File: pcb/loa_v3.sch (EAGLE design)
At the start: 111 parts, among them IC1 STM32F10XVXT6, IC2 M25P80MW, IC3 S34ML04G100TFI000, IC4 MCP1825S-1202E/DB, IC5 NCP3170, IC6 AD7265SU, Q2 50.000, Q3 25.000, U1 6SLX9TQG144, X3 MINI-USB

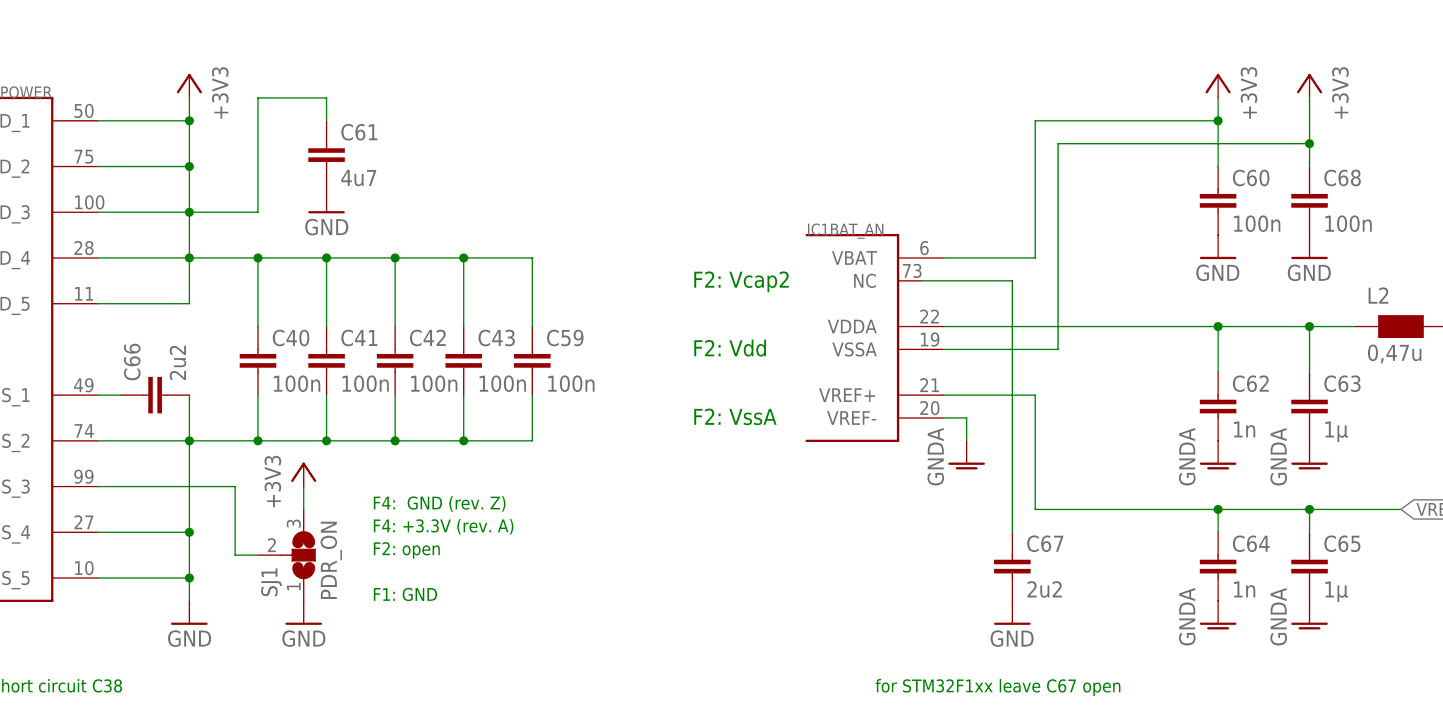
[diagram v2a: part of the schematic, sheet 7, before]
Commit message: Update NAND Flash Package, Reduces C type variations
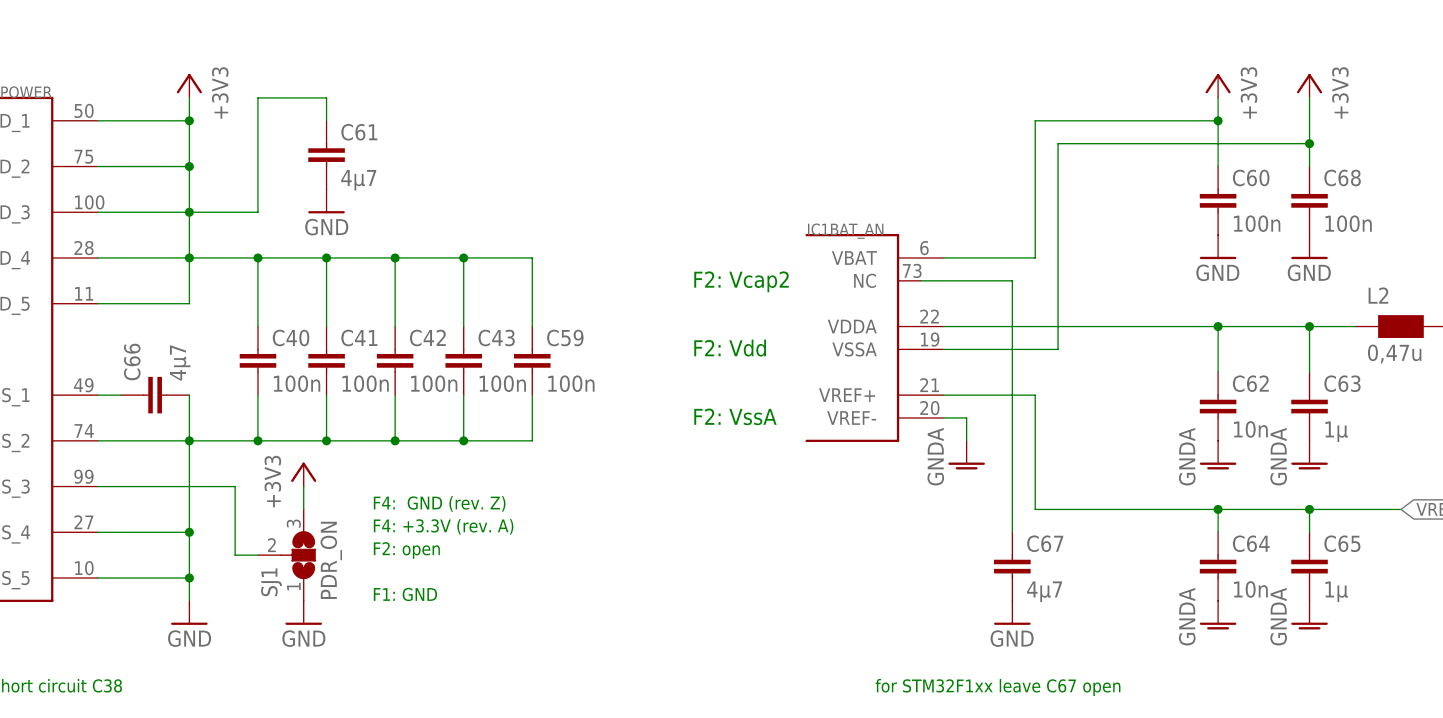
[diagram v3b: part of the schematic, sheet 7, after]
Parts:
- C61: value 4u7 -> 4µ7
- C62, C64: value 1n -> 10n
- C66, C67: value 2u2 -> 4µ7; REICHELT# X7R-G0805 2,2/25 -> X5R-G0805 4,7
- R1: value 820 -> 2k2
- R7: value 10k -> 2k2; device rcl:R-EU_R0603 -> rcl:R-EU_R0805
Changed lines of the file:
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@@
 <?xml version="1.0" encoding="utf-8"?>
 <!DOCTYPE eagle SYSTEM "eagle.dtd">
-<eagle version="6.4">
+<eagle version="6.5.0">
 <drawing>
 <settings>
@@
 <grid distance="0.1" unitdist="inch" unit="inch" style="lines" multiple="1" display="no" altdistance="0.01" altunitdist="inch" altunit="inch"/>
 <layers>
-<layer number="1" name="Top" color="4" fill="1" visible="no" active="no"/>
-<layer number="2" name="Route2" color="1" fill="3" visible="no" active="no"/>
-<layer number="3" name="Route3" color="11" fill="1" visible="no" active="no"/>
-<layer number="4" name="Route4" color="1" fill="4" visible="no" active="no"/>
-<layer number="5" name="Route5" color="4" fill="4" visible="no" active="no"/>
-<layer number="6" name="Route6" color="1" fill="8" visible="no" active="no"/>
-<layer number="7" name="Route7" color="4" fill="8" visible="no" active="no"/>
-<layer number="8" name="Route8" color="1" fill="2" visible="no" active="no"/>
-<layer number="9" name="Route9" color="4" fill="2" visible="no" active="no"/>
-<layer number="10" name="Route10" color="1" fill="7" visible="no" active="no"/>
-<layer number="11" name="Route11" color="4" fill="7" visible="no" active="no"/>
-<layer number="12" name="Route12" color="1" fill="5" visible="no" active="no"/>
-<layer number="13" name="Route13" color="4" fill="5" visible="no" active="no"/>
-<layer number="14" name="Route14" color="1" fill="6" visible="no" active="no"/>
-<layer number="15" name="Route15" color="11" fill="6" visible="no" active="no"/>
-<layer number="16" name="Bottom" color="1" fill="1" visible="no" active="no"/>
-<layer number="17" name="Pads" color="2" fill="1" visible="no" active="no"/>
-<layer number="18" name="Vias" color="2" fill="1" visible="no" active="no"/>
-<layer number="19" name="Unrouted" color="6" fill="1" visible="no" active="no"/>
-<layer number="20" name="Dimension" color="15" fill="1" visible="no" active="no"/>
-<layer number="21" name="tPlace" color="7" fill="1" visible="no" active="no"/>
-<layer number="22" name="bPlace" color="7" fill="1" visible="no" active="no"/>
-<layer number="23" name="tOrigins" color="15" fill="1" visible="no" active="no"/>
-<layer number="24" name="bOrigins" color="15" fill="1" visible="no" active="no"/>
-<layer number="25" name="tNames" color="7" fill="1" visible="no" active="no"/>
-<layer number="26" name="bNames" color="7" fill="1" visible="no" active="no"/>
-<layer number="27" name="tValues" color="7" fill="1" visible="no" active="no"/>
-<layer number="28" name="bValues" color="7" fill="1" visible="no" active="no"/>
+<layer number="1" name="Top" color="4" fill="1" visible="yes" active="no"/>
+<layer number="2" name="Route2" color="1" fill="3" visible="yes" active="no"/>
+<layer number="3" name="Route3" color="11" fill="1" visible="yes" active="no"/>
+<layer number="4" name="Route4" color="1" fill="4" visible="yes" active="no"/>
+<layer number="5" name="Route5" color="4" fill="4" visible="yes" active="no"/>
+<layer number="6" name="Route6" color="1" fill="8" visible="yes" active="no"/>
+<layer number="7" name="Route7" color="4" fill="8" visible="yes" active="no"/>
+<layer number="8" name="Route8" color="1" fill="2" visible="yes" active="no"/>
+<layer number="9" name="Route9" color="4" fill="2" visible="yes" active="no"/>
+<layer number="10" name="Route10" color="1" fill="7" visible="yes" active="no"/>
+<layer number="11" name="Route11" color="4" fill="7" visible="yes" active="no"/>
+<layer number="12" name="Route12" color="1" fill="5" visible="yes" active="no"/>
+<layer number="13" name="Route13" color="4" fill="5" visible="yes" active="no"/>
+<layer number="14" name="Route14" color="1" fill="6" visible="yes" active="no"/>
+<layer number="15" name="Route15" color="11" fill="6" visible="yes" active="no"/>
+<layer number="16" name="Bottom" color="1" fill="1" visible="yes" active="no"/>
+<layer number="17" name="Pads" color="2" fill="1" visible="yes" active="no"/>
+<layer number="18" name="Vias" color="2" fill="1" visible="yes" active="no"/>
+<layer number="19" name="Unrouted" color="6" fill="1" visible="yes" active="no"/>
+<layer number="20" name="Dimension" color="15" fill="1" visible="yes" active="no"/>
+<layer number="21" name="tPlace" color="7" fill="1" visible="yes" active="no"/>
+<layer number="22" name="bPlace" color="7" fill="1" visible="yes" active="no"/>
+<layer number="23" name="tOrigins" color="15" fill="1" visible="yes" active="no"/>
+<layer number="24" name="bOrigins" color="15" fill="1" visible="yes" active="no"/>
+<layer number="25" name="tNames" color="7" fill="1" visible="yes" active="no"/>
+<layer number="26" name="bNames" color="7" fill="1" visible="yes" active="no"/>
+<layer number="27" name="tValues" color="7" fill="1" visible="yes" active="no"/>
+<layer number="28" name="bValues" color="7" fill="1" visible="yes" active="no"/>
 <layer number="29" name="tStop" color="7" fill="3" visible="no" active="no"/>
 <layer number="30" name="bStop" color="7" fill="6" visible="no" active="no"/>
@@
 <layer number="35" name="tGlue" color="7" fill="4" visible="no" active="no"/>
 <layer number="36" name="bGlue" color="7" fill="5" visible="no" active="no"/>
-<layer number="37" name="tTest" color="7" fill="1" visible="no" active="no"/>
-<layer number="38" name="bTest" color="7" fill="1" visible="no" active="no"/>
+<layer number="37" name="tTest" color="7" fill="1" visible="yes" active="no"/>
+<layer number="38" name="bTest" color="7" fill="1" visible="yes" active="no"/>
 <layer number="39" name="tKeepout" color="4" fill="11" visible="no" active="no"/>
 <layer number="40" name="bKeepout" color="1" fill="11" visible="no" active="no"/>
@@
 <layer number="44" name="Drills" color="7" fill="1" visible="no" active="no"/>
 <layer number="45" name="Holes" color="7" fill="1" visible="no" active="no"/>
-<layer number="46" name="Milling" color="3" fill="1" visible="no" active="no"/>
-<layer number="47" name="Measures" color="7" fill="1" visible="no" active="no"/>
-<layer number="48" name="Document" color="7" fill="1" visible="no" active="no"/>
-<layer number="49" name="Reference" color="7" fill="1" visible="no" active="no"/>
-<layer number="50" name="dxf" color="7" fill="1" visible="no" active="no"/>
-<layer number="51" name="tDocu" color="7" fill="1" visible="no" active="no"/>
-<layer number="52" name="bDocu" color="7" fill="1" visible="no" active="no"/>
-<layer number="53" name="tGND_GNDA" color="7" fill="9" visible="no" active="no"/>
-<layer number="54" name="bGND_GNDA" color="1" fill="9" visible="no" active="no"/>
-<layer number="56" name="wert" color="7" fill="1" visible="no" active="no"/>
+<layer number="46" name="Milling" color="3" fill="1" visible="yes" active="no"/>
+<layer number="47" name="Measures" color="7" fill="1" visible="yes" active="no"/>
+<layer number="48" name="Document" color="7" fill="1" visible="yes" active="no"/>
+<layer number="49" name="Reference" color="7" fill="1" visible="yes" active="no"/>
+<layer number="50" name="dxf" color="7" fill="1" visible="yes" active="no"/>
+<layer number="51" name="tDocu" color="7" fill="1" visible="yes" active="no"/>
+<layer number="52" name="bDocu" color="7" fill="1" visible="yes" active="no"/>
+<layer number="53" name="tGND_GNDA" color="7" fill="9" visible="yes" active="no"/>
+<layer number="54" name="bGND_GNDA" color="1" fill="9" visible="yes" active="no"/>
+<layer number="56" name="wert" color="7" fill="1" visible="yes" active="no"/>
 <layer number="91" name="Nets" color="2" fill="1" visible="yes" active="yes"/>
 <layer number="92" name="Busses" color="1" fill="1" visible="yes" active="yes"/>
@@
 <part name="+3V53" library="supply1" deviceset="+3V3" device=""/>
 <part name="+3V54" library="supply1" deviceset="+3V3" device=""/>
-<part name="R7" library="rcl" deviceset="R-EU_" device="R0603" value="10k"/>
+<part name="R7" library="rcl" deviceset="R-EU_" device="R0805" value="2k2"/>
 <part name="GND25" library="supply1" deviceset="GND" device=""/>
 <part name="R11" library="rcl" deviceset="R-EU_" device="R0603" value="330"/>
@@
 <attribute name="REICHELT#" value="SMD-LED 0805 BL"/>
 </part>
-<part name="R1" library="rcl" deviceset="R-EU_" device="R0805" value="820"/>
+<part name="R1" library="rcl" deviceset="R-EU_" device="R0805" value="2k2"/>
 <part name="GND71" library="supply1" deviceset="GND" device=""/>
 <part name="GND93" library="supply1" deviceset="GND" device=""/>
@@
 <part name="GND12" library="supply1" deviceset="GND" device=""/>
 <part name="+3V12" library="supply1" deviceset="+3V3" device=""/>
-<part name="C61" library="rcl" deviceset="C-EU" device="C0805" value="4u7">
+<part name="C61" library="rcl" deviceset="C-EU" device="C0805" value="4µ7">
 <attribute name="REICHELT#" value="X5R-G0805 4,7"/>
 </part>
 <part name="GND13" library="supply1" deviceset="GND" device=""/>
-<part name="C62" library="rcl" deviceset="C-EU" device="C0603" value="1n">
+<part name="C62" library="rcl" deviceset="C-EU" device="C0603" value="10n">
 <attribute name="REICHELT#" value="X7R-G0603 1,0N"/>
 </part>
@@
 <attribute name="REICHELT#" value="X7R-G0805 1,0/25"/>
 </part>
-<part name="C64" library="rcl" deviceset="C-EU" device="C0603" value="1n">
+<part name="C64" library="rcl" deviceset="C-EU" device="C0603" value="10n">
 <attribute name="REICHELT#" value="X7R-G0603 1,0N"/>
 </part>
@@
 </part>
 <part name="+3V14" library="supply1" deviceset="+3V3" device=""/>
-<part name="C66" library="rcl" deviceset="C-EU" device="C0805" value="2u2">
-<attribute name="REICHELT#" value="X7R-G0805 2,2/25"/>
-</part>
-<part name="C67" library="rcl" deviceset="C-EU" device="C0805" value="2u2">
-<attribute name="REICHELT#" value="X7R-G0805 2,2/25"/>
+<part name="C66" library="rcl" deviceset="C-EU" device="C0805" value="4µ7">
+<attribute name="REICHELT#" value="X5R-G0805 4,7"/>
+</part>
+<part name="C67" library="rcl" deviceset="C-EU" device="C0805" value="4µ7">
+<attribute name="REICHELT#" value="X5R-G0805 4,7"/>
 </part>
 <part name="GND14" library="supply1" deviceset="GND" device=""/>
